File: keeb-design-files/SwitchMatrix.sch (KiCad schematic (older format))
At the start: 136 parts, among them SW10 8, SW11 9, SW12 0, SW13 -, SW14 =, SW15 BACKSPACE, SW16 HOME, SW2 `, SW3 1, SW4 2, SW5 3, SW6 4, SW7 5, SW8 6, SW9 7

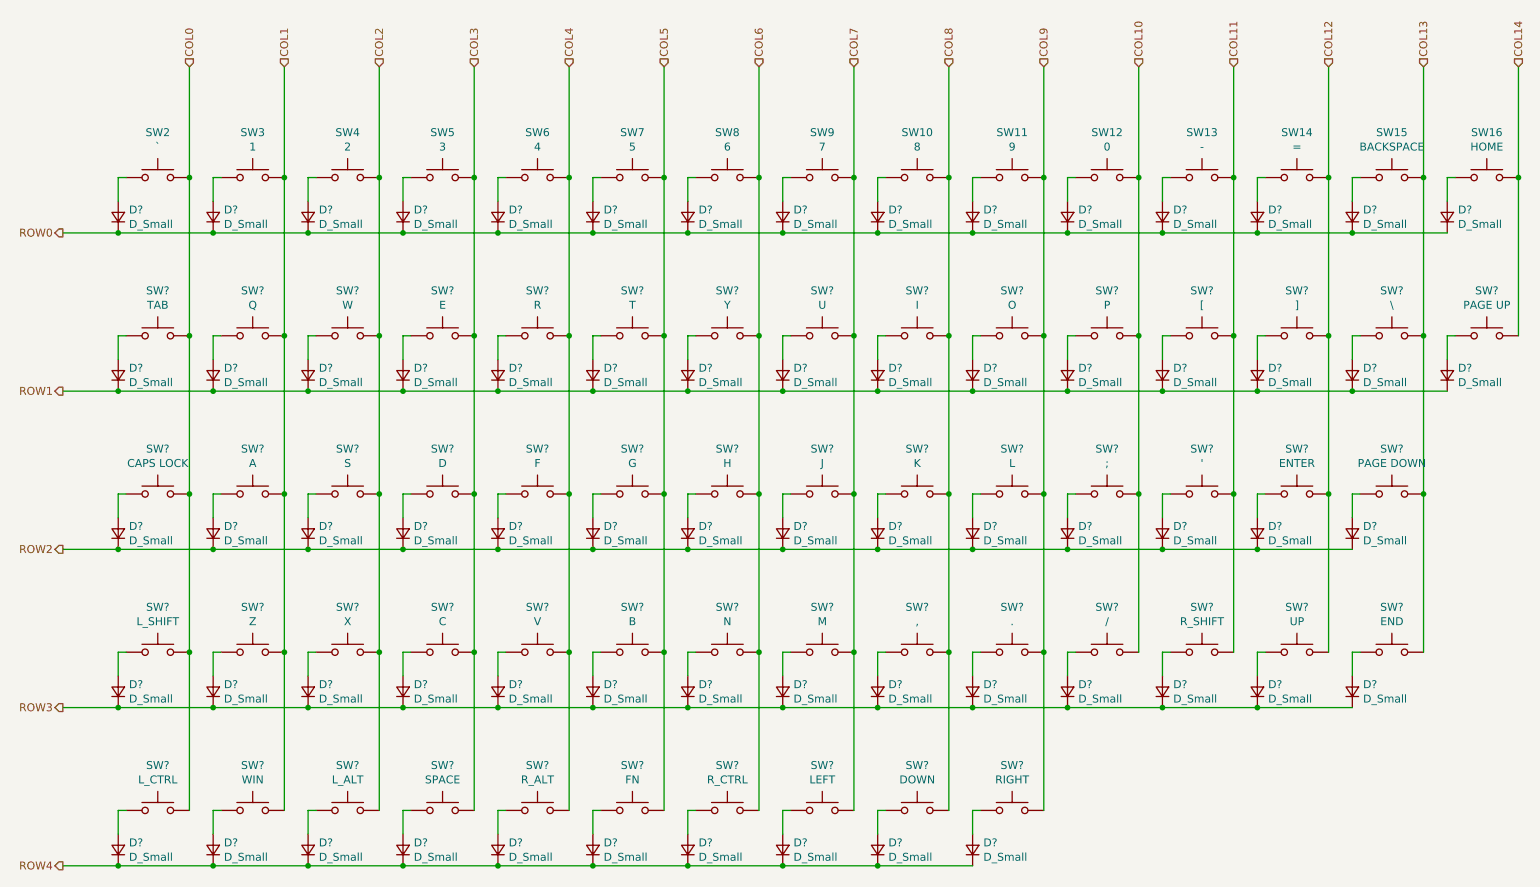
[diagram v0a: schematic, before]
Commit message: Add new Crystal and match symbols and footprints for switches and diodes
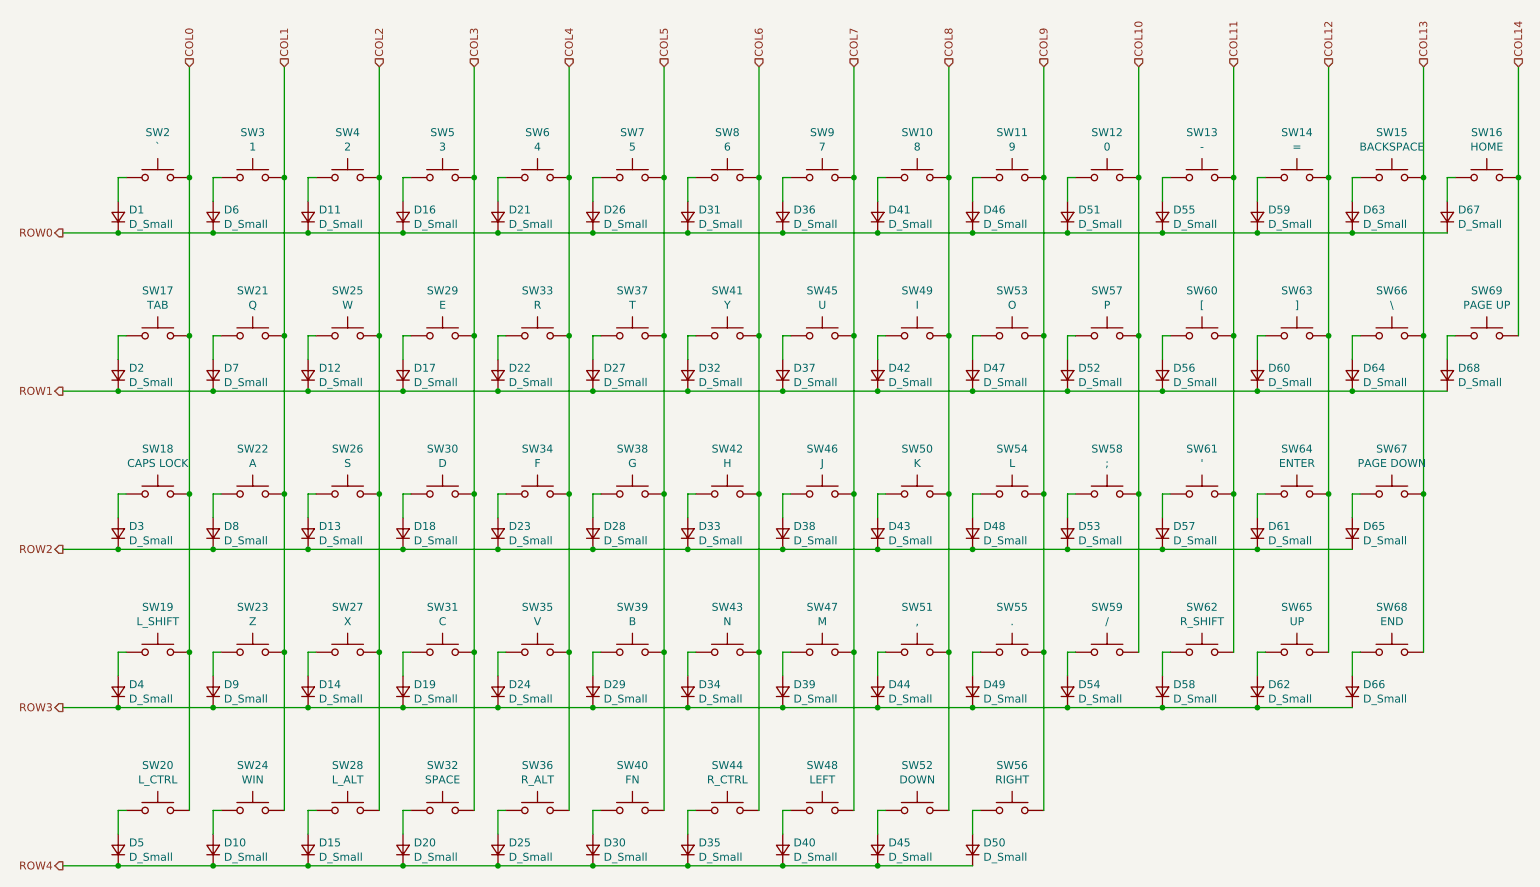
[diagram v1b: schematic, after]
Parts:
- D1, D10, D11, D12, D13, D14, D15, D16, D17, D18, D19, D2, D20, D21, D22, D23, D24, D25, D26, D27, D28, D29, D3, D30, D31, D32, D33, D34, D35, D36, D37, D38, D39, D4, D40, D41, D42, D43, D44, D45, D46, D47, D48, D49, D5, D50, D51, D52, D53, D54, D55, D56, D57, D58, D59, D6, D60, D61, D62, D63, D64, D65, D66, D67, D68, D7, D8, D9: renamed from D?; footprint (none) -> Diode_SMD:D_SOD-323_HandSoldering
- SW10, SW11, SW12, SW13, SW14, SW16, SW2, SW3, SW4, SW5, SW6, SW7, SW8, SW9: footprint (none) -> MX_Only:MXOnly-1U-Hotswap
- SW15: footprint (none) -> MX_Only:MXOnly-2U-Hotswap
- SW17, SW66: renamed from SW?; footprint (none) -> MX_Only:MXOnly-1.5U-Hotswap
- SW18, SW62: renamed from SW?; footprint (none) -> MX_Only:MXOnly-1.75U-Hotswap
- SW19, SW64: renamed from SW?; footprint (none) -> MX_Only:MXOnly-2.25U-Hotswap
- SW20, SW24, SW28: renamed from SW?; footprint (none) -> MX_Only:MXOnly-1.25U-Hotswap
- SW21, SW22, SW23, SW25, SW26, SW27, SW29, SW30, SW31, SW33, SW34, SW35, SW36, SW37, SW38, SW39, SW40, SW41, SW42, SW43, SW44, SW45, SW46, SW47, SW48, SW49, SW50, SW51, SW52, SW53, SW54, SW55, SW56, SW57, SW58, SW59, SW60, SW61, SW63, SW65, SW67, SW68, SW69: renamed from SW?; footprint (none) -> MX_Only:MXOnly-1U-Hotswap
- SW32: renamed from SW?; footprint (none) -> MX_Only:MXOnly-6.25U-Hotswap

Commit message: Confirm LCSC part numbers, started placement for layout
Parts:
- D1, D10, D11, D12, D13, D14, D15, D16, D17, D18, D19, D2, D20, D21, D22, D23, D24, D25, D26, D27, D28, D29, D3, D30, D31, D32, D33, D34, D35, D36, D37, D38, D39, D4, D40, D41, D42, D43, D44, D45, D46, D47, D48, D49, D5, D50, D51, D52, D53, D54, D55, D56, D57, D58, D59, D6, D60, D61, D62, D63, D64, D65, D66, D67, D68, D7, D8, D9: LCSC Part Number (none) -> C151442

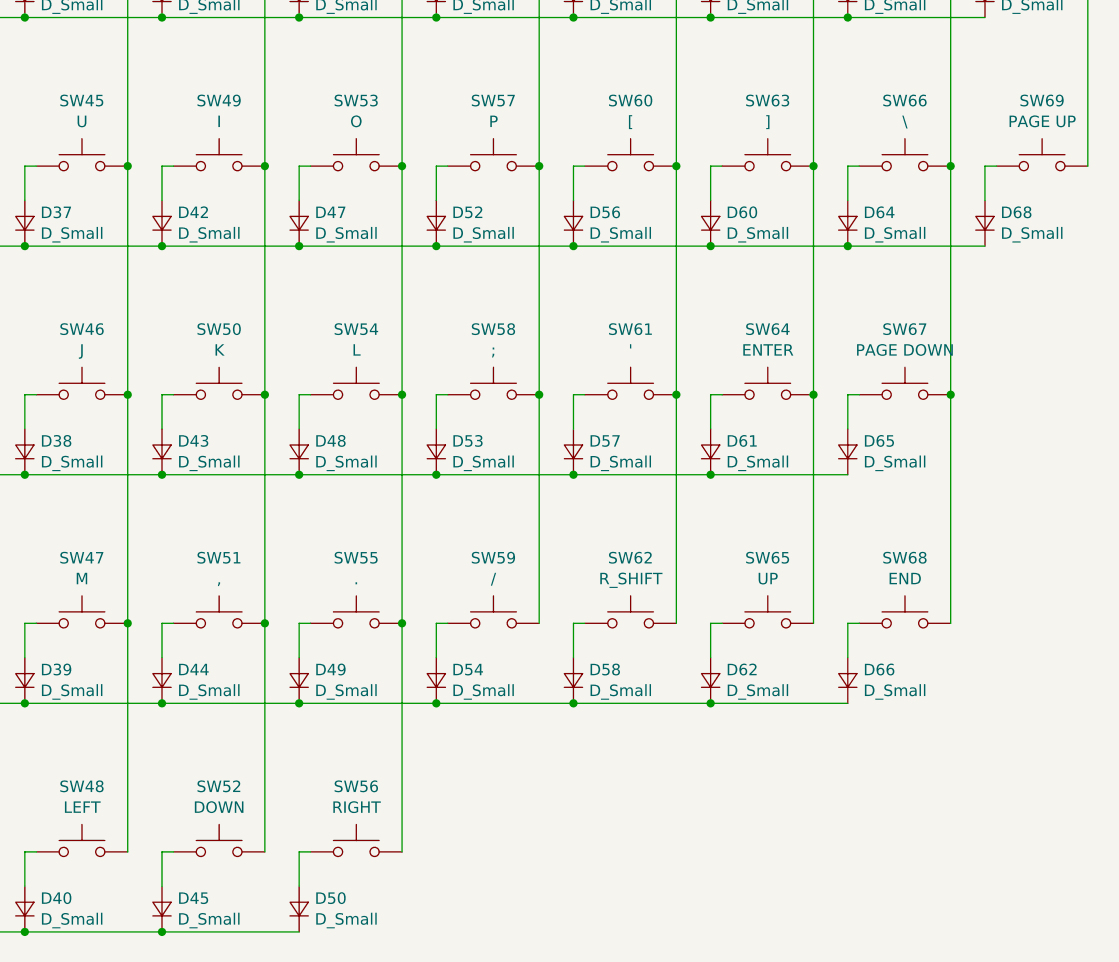
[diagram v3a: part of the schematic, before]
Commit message: Re-map MCU pins, Add LEDs, Remove USB Isolation cause it couldn't handle the POWER! More routing done
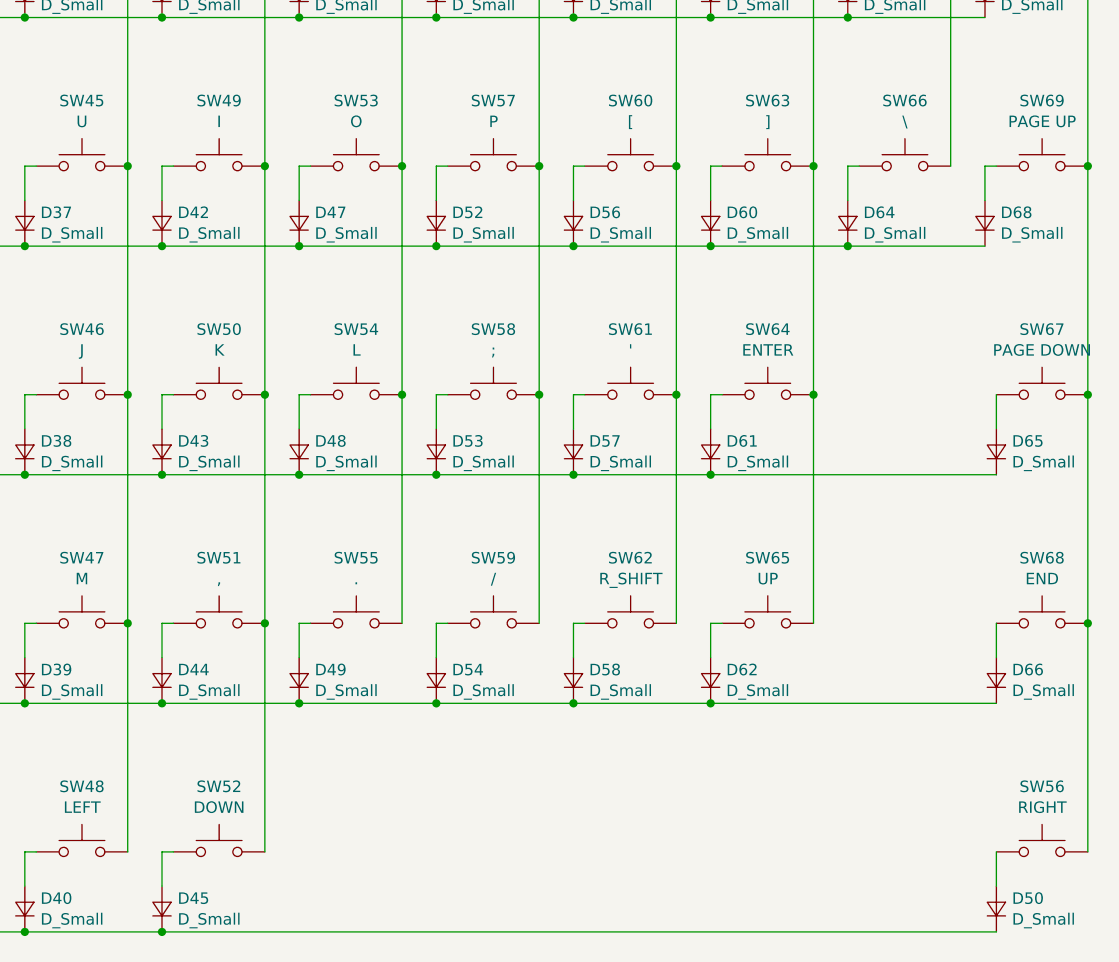
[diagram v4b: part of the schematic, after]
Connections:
- net COL13: no longer SW67.2, SW68.2
- net COL14: now also SW56.2, SW67.2, SW68.2
- net COL9: no longer SW56.2
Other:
- moved on the sheet: D50, D65, D66, SW56, SW67, SW68
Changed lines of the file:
@@
 L Switch:SW_Push SW67
 U 1 1 5EB63425
-P 9200 4000
-F 0 "SW67" H 9200 4285 50  0000 C CNN
-F 1 "PAGE DOWN" H 9200 4194 50  0000 C CNN
-F 2 "MX_Only:MXOnly-1U-Hotswap" H 9200 4200 50  0001 C CNN
-F 3 "~" H 9200 4200 50  0001 C CNN
-	1    9200 4000
+P 9800 4000
+F 0 "SW67" H 9800 4285 50  0000 C CNN
+F 1 "PAGE DOWN" H 9800 4194 50  0000 C CNN
+F 2 "MX_Only:MXOnly-1U-Hotswap" H 9800 4200 50  0001 C CNN
+F 3 "~" H 9800 4200 50  0001 C CNN
+	1    9800 4000
 	1    0    0    -1
 $EndComp
@@
 L Switch:SW_Push SW68
 U 1 1 5EB77D9F
-P 9200 5000
-F 0 "SW68" H 9200 5285 50  0000 C CNN
-F 1 "END" H 9200 5194 50  0000 C CNN
-F 2 "MX_Only:MXOnly-1U-Hotswap" H 9200 5200 50  0001 C CNN
-F 3 "~" H 9200 5200 50  0001 C CNN
-	1    9200 5000
+P 9800 5000
+F 0 "SW68" H 9800 5285 50  0000 C CNN
+F 1 "END" H 9800 5194 50  0000 C CNN
+F 2 "MX_Only:MXOnly-1U-Hotswap" H 9800 5200 50  0001 C CNN
+F 3 "~" H 9800 5200 50  0001 C CNN
+	1    9800 5000
 	1    0    0    -1
 $EndComp
@@
 L Switch:SW_Push SW56
 U 1 1 5EB7C6A7
-P 6800 6000
-F 0 "SW56" H 6800 6285 50  0000 C CNN
-F 1 "RIGHT" H 6800 6194 50  0000 C CNN
-F 2 "MX_Only:MXOnly-1U-Hotswap" H 6800 6200 50  0001 C CNN
-F 3 "~" H 6800 6200 50  0001 C CNN
-	1    6800 6000
+P 9800 6000
+F 0 "SW56" H 9800 6285 50  0000 C CNN
+F 1 "RIGHT" H 9800 6194 50  0000 C CNN
+F 2 "MX_Only:MXOnly-1U-Hotswap" H 9800 6200 50  0001 C CNN
+F 3 "~" H 9800 6200 50  0001 C CNN
+	1    9800 6000
 	1    0    0    -1
 $EndComp
@@
 Wire Wire Line
 	6400 5000 6400 6000
-Wire Wire Line
-	7000 6000 7000 5000
 Connection ~ 7000 2000
 Wire Wire Line
@@
 Wire Wire Line
 	7000 4000 7000 3000
-Connection ~ 7000 5000
 Wire Wire Line
 	7000 5000 7000 4000
@@
 Wire Wire Line
 	8800 3000 8800 4000
-Wire Wire Line
-	9400 4000 9400 3000
 Connection ~ 9400 2000
 Wire Wire Line
 	9400 2000 9400 1300
-Connection ~ 9400 3000
 Wire Wire Line
 	9400 3000 9400 2000
@@
 	8800 4000 8800 5000
 Connection ~ 8800 4000
-Wire Wire Line
-	9400 4000 9400 5000
-Connection ~ 9400 4000
 Text HLabel 800  3350 0    50   Output ~ 0
 ROW1
@@
 L Device:D_Small D65
 U 1 1 5ECFF6DC
-P 8950 4250
-F 0 "D65" V 8996 4182 50  0000 R CNN
-F 1 "D_Small" V 8905 4182 50  0000 R CNN
-F 2 "Diode_SMD:D_SOD-323_HandSoldering" V 8950 4250 50  0001 C CNN
-F 3 "~" V 8950 4250 50  0001 C CNN
-F 4 "C151442" H 8950 4250 50  0001 C CNN "LCSC Part Number"
-	1    8950 4250
+P 9600 4250
+F 0 "D65" V 9646 4182 50  0000 R CNN
+F 1 "D_Small" V 9555 4182 50  0000 R CNN
+F 2 "Diode_SMD:D_SOD-323_HandSoldering" V 9600 4250 50  0001 C CNN
+F 3 "~" V 9600 4250 50  0001 C CNN
+F 4 "C151442" H 9600 4250 50  0001 C CNN "LCSC Part Number"
+	1    9600 4250
 	0    -1   -1   0
 $EndComp
@@
 Wire Wire Line
 	8350 4000 8350 4150
-Wire Wire Line
-	9000 4000 8950 4000
-Wire Wire Line
-	8950 4000 8950 4150
 Text HLabel 800  4350 0    50   Output ~ 0
 ROW2
@@
 Wire Wire Line
 	7750 4350 8350 4350
-Connection ~ 8350 4350
-Wire Wire Line
-	8350 4350 8950 4350
 $Comp
 L Device:D_Small D4
@@
 L Device:D_Small D66
 U 1 1 5EDE6DEB
-P 8950 5250
-F 0 "D66" V 8996 5182 50  0000 R CNN
-F 1 "D_Small" V 8905 5182 50  0000 R CNN
-F 2 "Diode_SMD:D_SOD-323_HandSoldering" V 8950 5250 50  0001 C CNN
-F 3 "~" V 8950 5250 50  0001 C CNN
-F 4 "C151442" H 8950 5250 50  0001 C CNN "LCSC Part Number"
-	1    8950 5250
-	0    -1   -1   0
-$EndComp
-Wire Wire Line
-	9000 5000 8950 5000
-Wire Wire Line
-	8950 5000 8950 5150
+P 9600 5250
+F 0 "D66" V 9646 5182 50  0000 R CNN
+F 1 "D_Small" V 9555 5182 50  0000 R CNN
+F 2 "Diode_SMD:D_SOD-323_HandSoldering" V 9600 5250 50  0001 C CNN
+F 3 "~" V 9600 5250 50  0001 C CNN
+F 4 "C151442" H 9600 5250 50  0001 C CNN "LCSC Part Number"
+	1    9600 5250
+	0    -1   -1   0
+$EndComp
 Wire Wire Line
 	8400 5000 8350 5000
@@
 	7750 5350 8350 5350
 Connection ~ 8350 5350
-Wire Wire Line
-	8350 5350 8950 5350
 $Comp
 L Device:D_Small D5
@@
 L Device:D_Small D50
 U 1 1 5EF28487
-P 6550 6250
-F 0 "D50" V 6596 6182 50  0000 R CNN
-F 1 "D_Small" V 6505 6182 50  0000 R CNN
-F 2 "Diode_SMD:D_SOD-323_HandSoldering" V 6550 6250 50  0001 C CNN
-F 3 "~" V 6550 6250 50  0001 C CNN
-F 4 "C151442" H 6550 6250 50  0001 C CNN "LCSC Part Number"
-	1    6550 6250
+P 9600 6250
+F 0 "D50" V 9646 6182 50  0000 R CNN
+F 1 "D_Small" V 9555 6182 50  0000 R CNN
+F 2 "Diode_SMD:D_SOD-323_HandSoldering" V 9600 6250 50  0001 C CNN
+F 3 "~" V 9600 6250 50  0001 C CNN
+F 4 "C151442" H 9600 6250 50  0001 C CNN "LCSC Part Number"
+	1    9600 6250
 	0    -1   -1   0
 $EndComp
@@
 Wire Wire Line
 	5950 6000 5950 6150
-Wire Wire Line
-	6600 6000 6550 6000
-Wire Wire Line
-	6550 6000 6550 6150
 Text HLabel 800  6350 0    50   Output ~ 0
 ROW4
@@
 Connection ~ 5950 6350
 Wire Wire Line
-	5950 6350 6550 6350
+	10000 3000 10000 4000
+Connection ~ 10000 3000
+Wire Wire Line
+	9600 4150 9600 4000
+Wire Wire Line
+	8350 4350 9600 4350
+Connection ~ 8350 4350
+Wire Wire Line
+	8350 5350 9600 5350
+Wire Wire Line
+	9600 5150 9600 5000
+Wire Wire Line
+	10000 4000 10000 5000
+Connection ~ 10000 4000
+Wire Wire Line
+	10000 5000 10000 6000
+Connection ~ 10000 5000
+Wire Wire Line
+	9600 6000 9600 6150
+Wire Wire Line
+	5950 6350 9600 6350
 $EndSCHEMATC
